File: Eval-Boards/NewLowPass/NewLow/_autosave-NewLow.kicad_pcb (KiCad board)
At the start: 2 copper layers, 31.5 x 24.6 mm, 5 parts

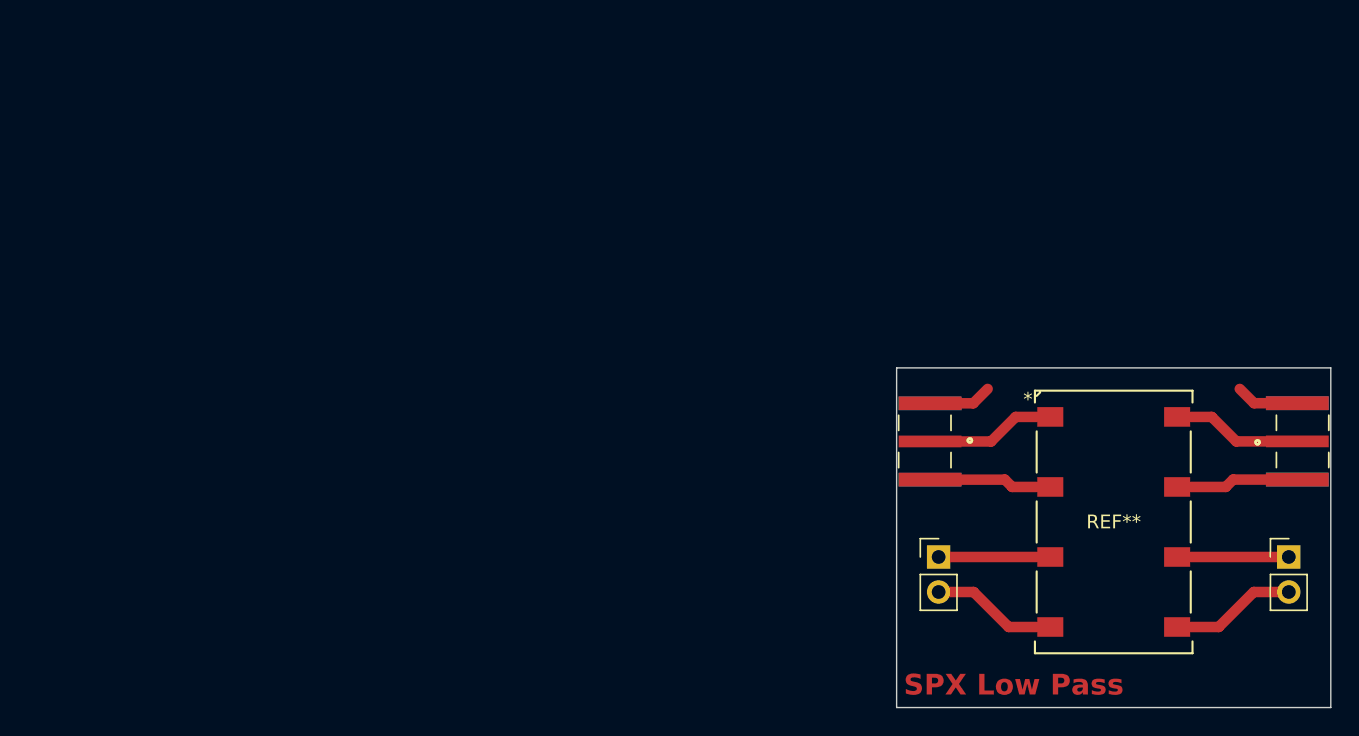
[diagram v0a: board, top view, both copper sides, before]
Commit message: Created new board for the Low pass even though it says bandpass stuff
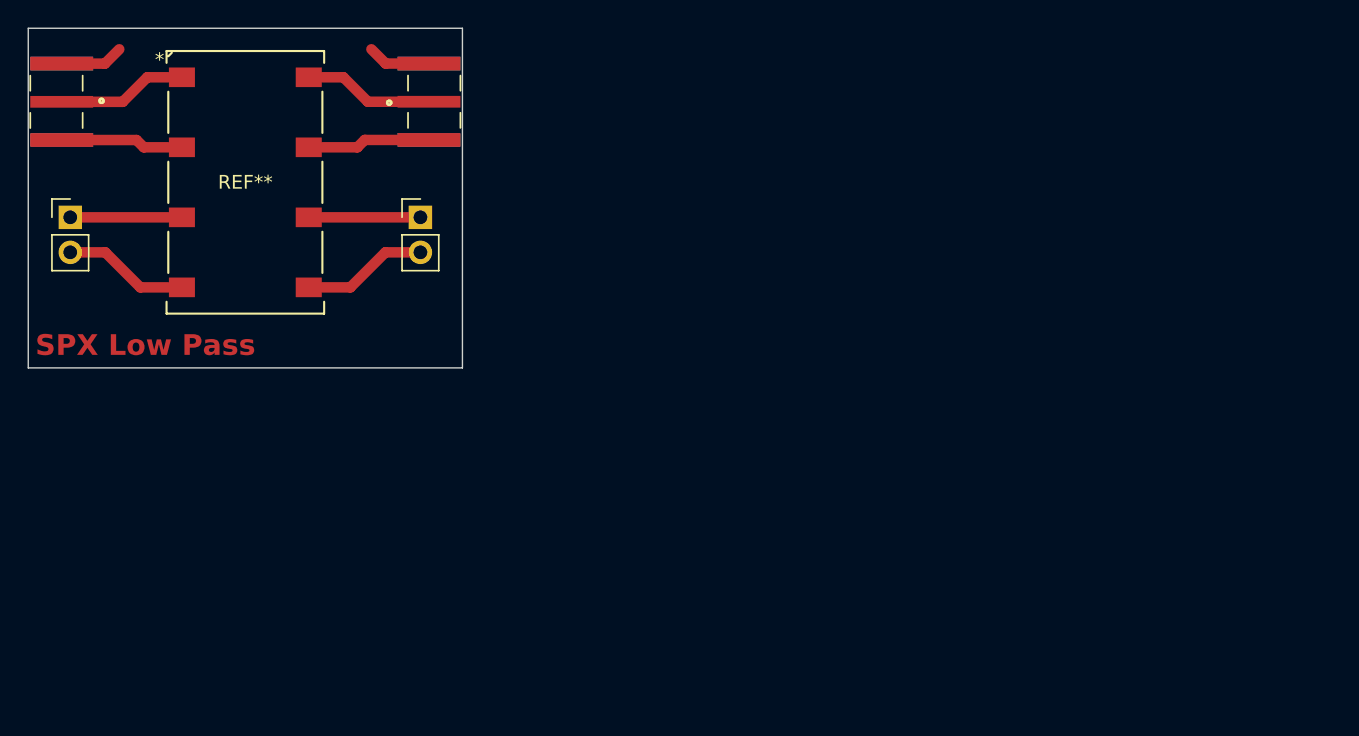
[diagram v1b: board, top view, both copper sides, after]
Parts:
- removed the REF** at (137.2, 96.5)
- removed the REF** at (162.6, 96.5)
- removed the REF** at (163.2, 88.1)
- removed the REF** at (136.5, 88.1)
- added REF**: TAOGLAS_EMPCB.SMAFSTJ.B.HT, SMA connectors:TAOGLAS_EMPCB.SMAFSTJ.B.HT, F.Cu at (100.2, 63.5)
- added REF**: TAOGLAS_EMPCB.SMAFSTJ.B.HT, SMA connectors:TAOGLAS_EMPCB.SMAFSTJ.B.HT, F.Cu at (73.5, 63.5)
- added REF**: PinHeader_1x02_P2.54mm_Vertical, Connector_PinHeader_2.54mm:PinHeader_1x02_P2.54mm_Vertical, F.Cu at (74.2, 71.9)
- added REF**: PinHeader_1x02_P2.54mm_Vertical, Connector_PinHeader_2.54mm:PinHeader_1x02_P2.54mm_Vertical, F.Cu at (99.6, 71.9)
- moved REF** 67.6 mm to (86.9, 69.3)
